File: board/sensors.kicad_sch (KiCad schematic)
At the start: 6 parts, among them U7 MAX-M10M

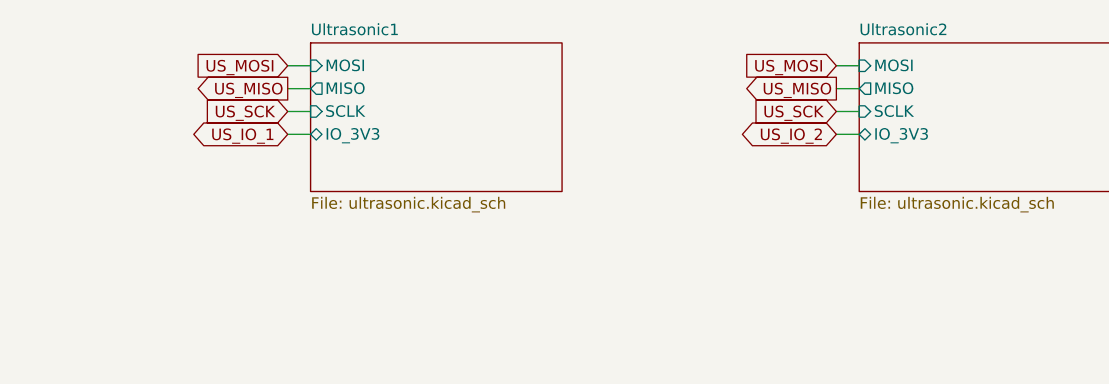
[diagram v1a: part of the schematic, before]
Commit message: Fixed full errata, now v2.1 Most important changes: * Changed power supply architecture * Added hardware ID resistors * Moved USB connector closer to/over the border * Added a 2A fuse * Replaced Beads to display with resistors for better signal integrity * Replaced IP5306 with IP5303 for lower charging current * Switched PGA sensors from TCI to SPI, removed TCI/IO connection * Switched PGA mode from temperature to time decoupling * Added a power-on-reset circuit to keep power-consumption low due to voltage on 5V rail if turned off * Retracted copper planes from the PCB border * Added fabrication output using KiCAD JLCPCB tools
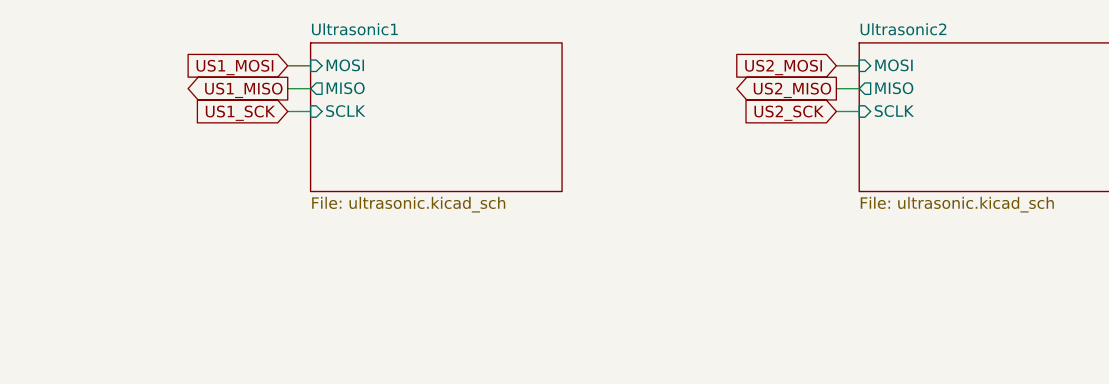
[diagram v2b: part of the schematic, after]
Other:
- sheet Ultrasonic1 ports: added none; removed IO_3V3
- sheet Ultrasonic2 ports: added none; removed IO_3V3
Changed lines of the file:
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@@
-    (stroke (width 0) (type default))
-  )
-  (wire (pts (xy 72.39 50.8) (xy 74.93 50.8))
     (stroke (width 0) (type default))
   )
@@
   )
   (wire (pts (xy 80.01 95.25) (xy 80.01 96.52))
-    (stroke (width 0) (type default))
-  )
-  (wire (pts (xy 133.35 50.8) (xy 135.89 50.8))
     (stroke (width 0) (type default))
   )
@@
     (effects (font (size 1.27 1.27)) (justify left bottom))
   )
-  (global_label "US_MISO" (shape output) (at 133.35 45.72 180) (fields_autoplaced)
-    (effects (font (size 1.27 1.27)) (justify right))
-    (property "Intersheetrefs" "${INTERSHEET_REFS}" (at 122.261 45.72 0)
-      (effects (font (size 1.27 1.27)) (justify right) hide)
-    )
-  )
-  (global_label "US_IO_1" (shape bidirectional) (at 72.39 50.8 180) (fields_autoplaced)
-    (effects (font (size 1.27 1.27)) (justify right))
-    (property "Intersheetrefs" "${INTERSHEET_REFS}" (at 60.6735 50.8 0)
-      (effects (font (size 1.27 1.27)) (justify right) hide)
-    )
-  )
-  (global_label "US_SCK" (shape input) (at 133.35 48.26 180) (fields_autoplaced)
-    (effects (font (size 1.27 1.27)) (justify right))
-    (property "Intersheetrefs" "${INTERSHEET_REFS}" (at 123.1077 48.26 0)
-      (effects (font (size 1.27 1.27)) (justify right) hide)
-    )
-  )
-  (global_label "US_IO_2" (shape bidirectional) (at 133.35 50.8 180) (fields_autoplaced)
-    (effects (font (size 1.27 1.27)) (justify right))
-    (property "Intersheetrefs" "${INTERSHEET_REFS}" (at 121.6335 50.8 0)
-      (effects (font (size 1.27 1.27)) (justify right) hide)
-    )
-  )
-  (global_label "US_MOSI" (shape input) (at 133.35 43.18 180) (fields_autoplaced)
-    (effects (font (size 1.27 1.27)) (justify right))
-    (property "Intersheetrefs" "${INTERSHEET_REFS}" (at 122.261 43.18 0)
-      (effects (font (size 1.27 1.27)) (justify right) hide)
-    )
-  )
-  (global_label "US_MOSI" (shape input) (at 72.39 43.18 180) (fields_autoplaced)
-    (effects (font (size 1.27 1.27)) (justify right))
-    (property "Intersheetrefs" "${INTERSHEET_REFS}" (at 61.301 43.18 0)
+  (global_label "US2_MISO" (shape output) (at 133.35 45.72 180) (fields_autoplaced)
+    (effects (font (size 1.27 1.27)) (justify right))
+    (property "Intersheetrefs" "${INTERSHEET_REFS}" (at 121.0515 45.72 0)
+      (effects (font (size 1.27 1.27)) (justify right) hide)
+    )
+  )
+  (global_label "US2_SCK" (shape input) (at 133.35 48.26 180) (fields_autoplaced)
+    (effects (font (size 1.27 1.27)) (justify right))
+    (property "Intersheetrefs" "${INTERSHEET_REFS}" (at 121.8982 48.26 0)
+      (effects (font (size 1.27 1.27)) (justify right) hide)
+    )
+  )
+  (global_label "US2_MOSI" (shape input) (at 133.35 43.18 180) (fields_autoplaced)
+    (effects (font (size 1.27 1.27)) (justify right))
+    (property "Intersheetrefs" "${INTERSHEET_REFS}" (at 121.0515 43.18 0)
+      (effects (font (size 1.27 1.27)) (justify right) hide)
+    )
+  )
+  (global_label "US1_MOSI" (shape input) (at 72.39 43.18 180) (fields_autoplaced)
+    (effects (font (size 1.27 1.27)) (justify right))
+    (property "Intersheetrefs" "${INTERSHEET_REFS}" (at 60.0915 43.18 0)
       (effects (font (size 1.27 1.27)) (justify right) hide)
     )
@@
     )
   )
-  (global_label "US_SCK" (shape input) (at 72.39 48.26 180) (fields_autoplaced)
-    (effects (font (size 1.27 1.27)) (justify right))
-    (property "Intersheetrefs" "${INTERSHEET_REFS}" (at 62.1477 48.26 0)
-      (effects (font (size 1.27 1.27)) (justify right) hide)
-    )
-  )
-  (global_label "US_MISO" (shape output) (at 72.39 45.72 180) (fields_autoplaced)
-    (effects (font (size 1.27 1.27)) (justify right))
-    (property "Intersheetrefs" "${INTERSHEET_REFS}" (at 61.301 45.72 0)
+  (global_label "US1_SCK" (shape input) (at 72.39 48.26 180) (fields_autoplaced)
+    (effects (font (size 1.27 1.27)) (justify right))
+    (property "Intersheetrefs" "${INTERSHEET_REFS}" (at 60.9382 48.26 0)
+      (effects (font (size 1.27 1.27)) (justify right) hide)
+    )
+  )
+  (global_label "US1_MISO" (shape output) (at 72.39 45.72 180) (fields_autoplaced)
+    (effects (font (size 1.27 1.27)) (justify right))
+    (property "Intersheetrefs" "${INTERSHEET_REFS}" (at 60.0915 45.72 0)
       (effects (font (size 1.27 1.27)) (justify right) hide)
     )
@@
       (effects (font (size 1.27 1.27)) (justify left))
     )
-    (pin "IO_3V3" bidirectional (at 74.93 50.8 180)
-      (effects (font (size 1.27 1.27)) (justify left))
-    )
     (instances
       (project "OBSPro"
@@
       (effects (font (size 1.27 1.27)) (justify left))
     )
-    (pin "IO_3V3" bidirectional (at 135.89 50.8 180)
-      (effects (font (size 1.27 1.27)) (justify left))
-    )

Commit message: Hardware Revision
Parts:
- removed AE1: Antenna_Chip, OBSPro:GPS1003, symbol Device:Antenna_Chip
- added J7: U.FL GPS, symbol Connector:Conn_Coaxial
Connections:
- net ANT: now also J7.1 (In)
- net GND: now also J7.2 (Ext)
- no-connect marks 10 -> 9

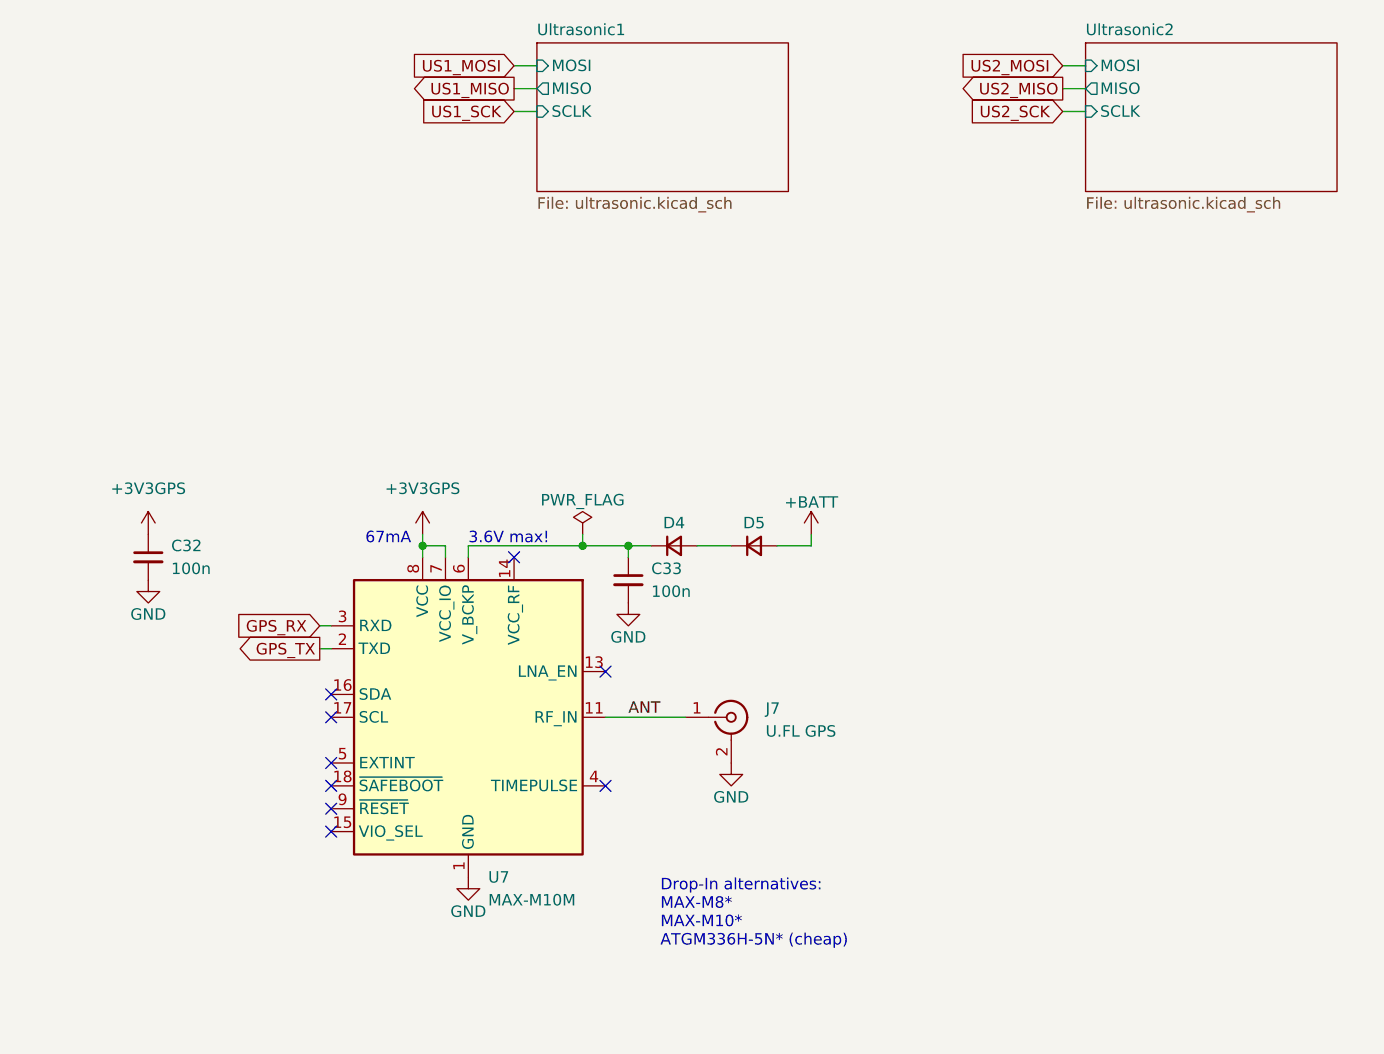
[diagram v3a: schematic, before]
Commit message: Fix errors in schematic for new board design
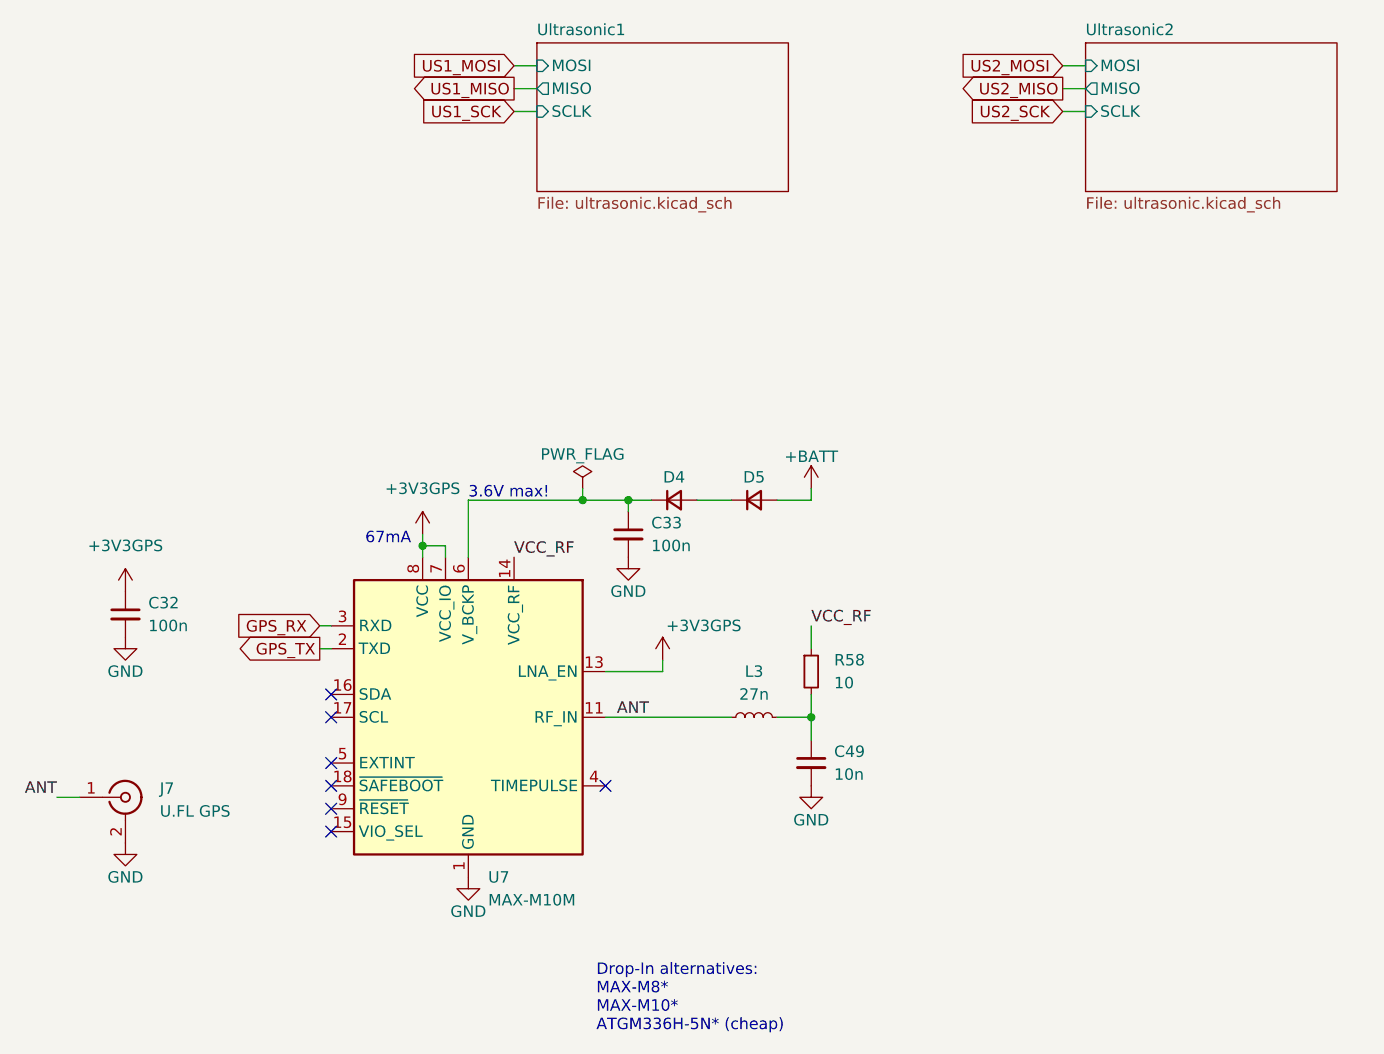
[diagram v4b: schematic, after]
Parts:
- added C49: 10n, Capacitor_SMD:C_0603_1608Metric, symbol Device:C_Small
- added L3: 27n, Inductor_SMD:L_0603_1608Metric, symbol Device:L_Small
- added R58: 10, Resistor_SMD:R_1206_3216Metric, symbol Device:R_Small
- J7: footprint (none) -> Connector_Coaxial:U.FL_Hirose_U.FL-R-SMT-1_Vertical; JLC_PN (none) -> C5137195
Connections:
- net +3V3GPS: now also U7.13 (LNA_EN)
- net ANT: now also L3.1
- net GND: now also C49.2
- net VCC_RF: now reaches U7.14 (VCC_RF)
- net VCC_RF: now also R58.1
- new net: C49.1, L3.2, R58.2
- no-connect marks 9 -> 7
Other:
- moved on the sheet: C32, C33, D4, D5, J7

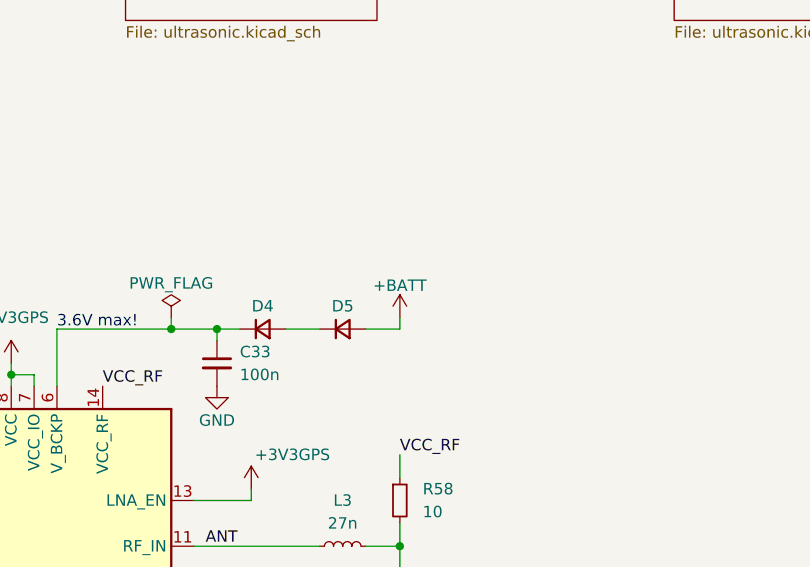
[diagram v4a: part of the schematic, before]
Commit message: Update schematic and PCB layout
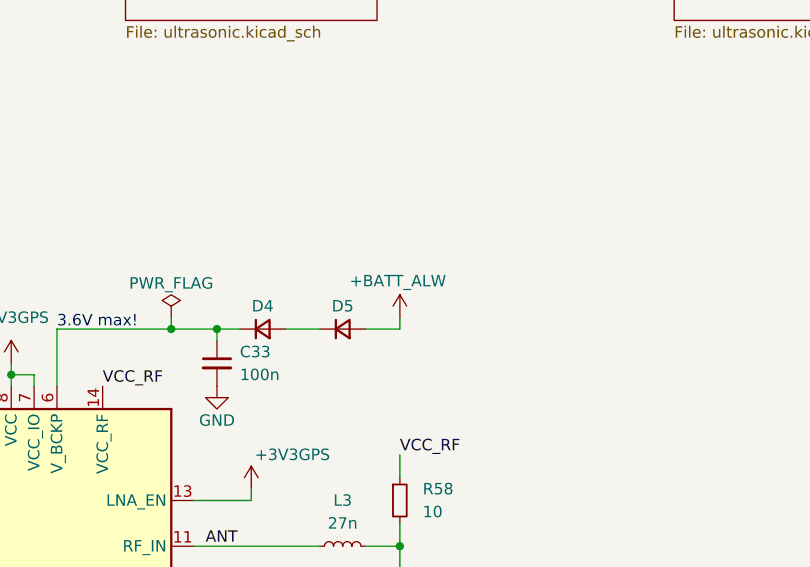
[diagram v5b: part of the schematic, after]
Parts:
- R58: footprint Resistor_SMD:R_1206_3216Metric -> Resistor_SMD:R_0603_1608Metric; JLC_PN C25349 -> C22859; MPN 1206W4J0100T5E -> 0603WAF100JT5E
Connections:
- net +BATT renamed +BATT_ALW
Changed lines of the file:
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@@
 		(on_board yes)
 		(dnp no)
-		(fields_autoplaced yes)
 		(property "Reference" "#PWR090"
 			(at 105.41 93.98 0)
@@
 			)
 		)
-		(property "Value" "+BATT"
-			(at 105.41 86.614 0)
+		(property "Value" "+BATT_ALW"
+			(at 99.822 86.106 0)
 			(effects
 				(font
 					(size 1.27 1.27)
 				)
+				(justify left)
 			)
 		)
@@
 			)
 		)
-		(property "Footprint" "Resistor_SMD:R_1206_3216Metric"
+		(property "Footprint" "Resistor_SMD:R_0603_1608Metric"
 			(at 105.41 110.49 0)
 			(effects
@@
 			)
 		)
-		(property "MPN" "1206W4J0100T5E"
+		(property "MPN" "0603WAF100JT5E"
 			(at 105.41 110.49 0)
 			(effects
@@
 			)
 		)
-		(property "JLC_PN" "C25349"
+		(property "JLC_PN" "C22859"
 			(at 105.41 110.49 0)
 			(effects
